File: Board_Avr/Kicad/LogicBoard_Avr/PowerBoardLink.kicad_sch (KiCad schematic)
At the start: 7 parts, among them J4 Power Board Connector

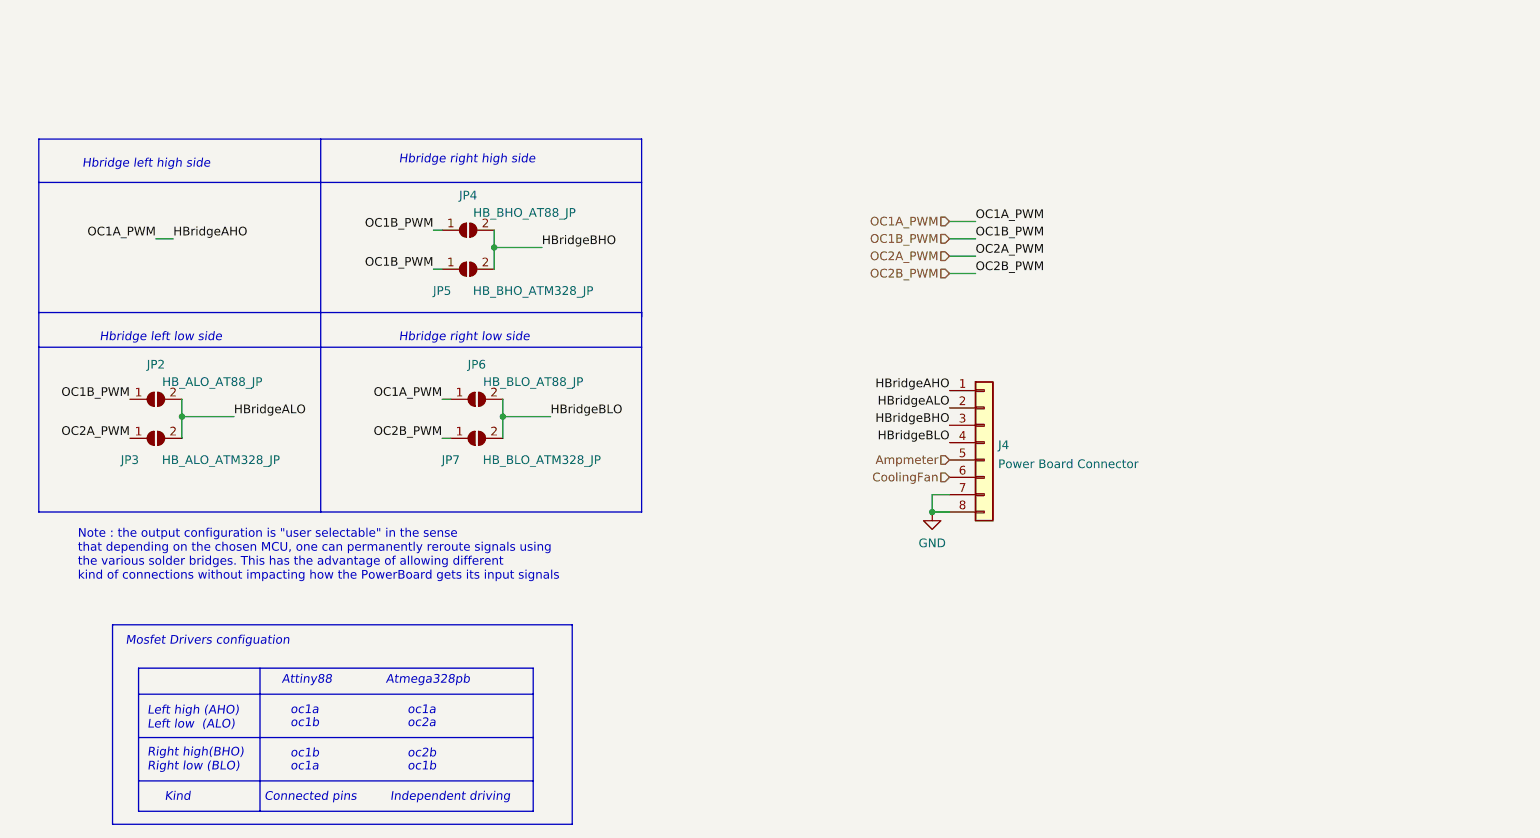
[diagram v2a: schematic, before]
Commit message: Started routing all traces
Signed-off-by: bebenlebricolo <benoittarrade@hotmail.fr>
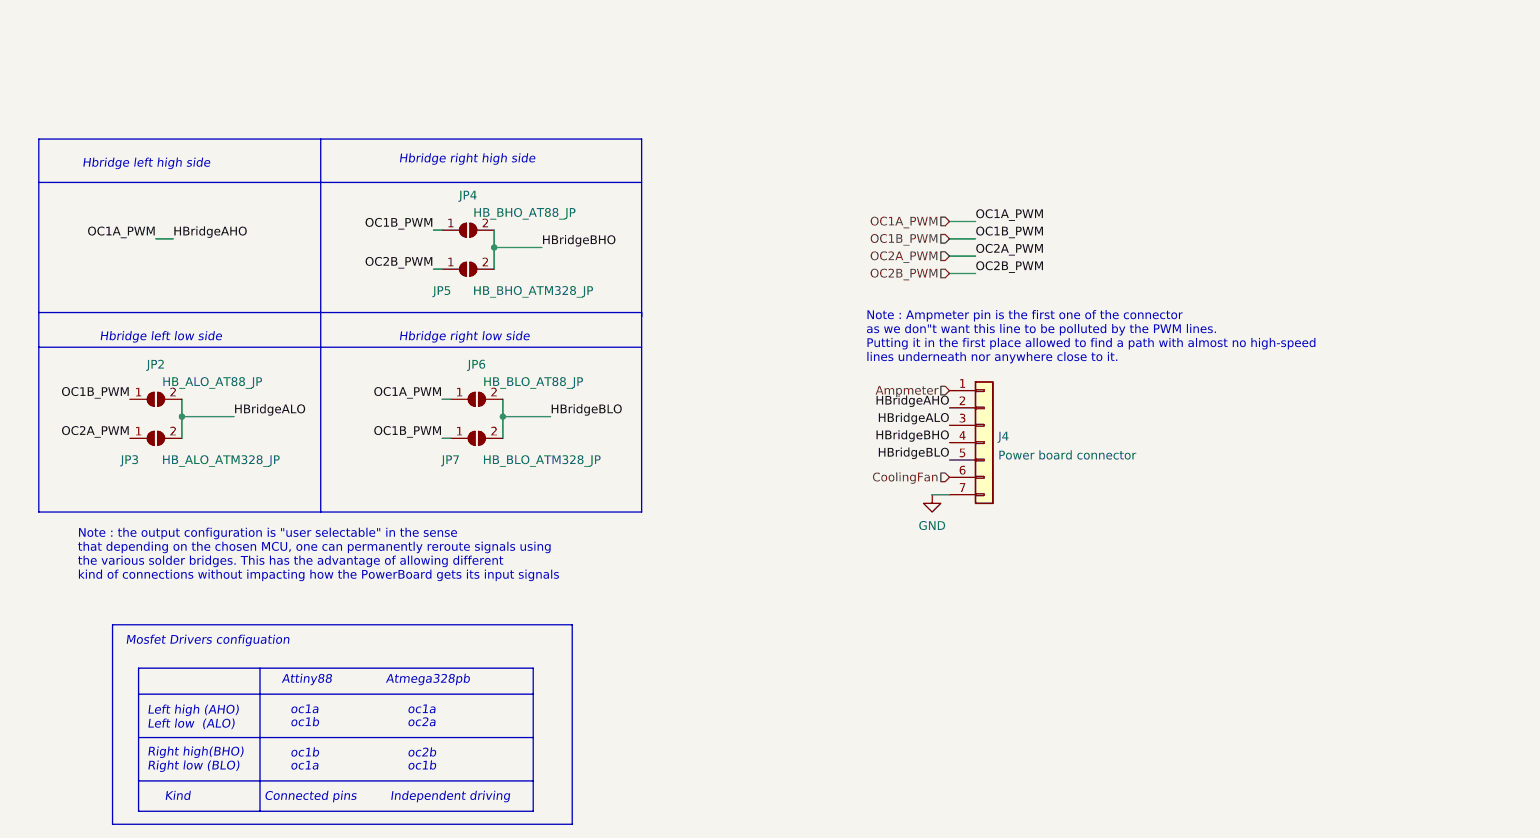
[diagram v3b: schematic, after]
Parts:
- removed J4: Power Board Connector, symbol Connector_Generic:Conn_01x08
- added J4: Power board connector, Connector_PinHeader_2.54mm:PinHeader_1x07_P2.54mm_Vertical, symbol Connector_Generic:Conn_01x07
- JP2, JP3, JP4, JP5, JP6, JP7: footprint (none) -> Jumper:SolderJumper-2_P1.3mm_Open_RoundedPad1.0x1.5mm
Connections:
- net Ampmeter: now also J4.1 (Pin_1)
- net CoolingFan: now also J4.6 (Pin_6)
- net GND: now also J4.7 (Pin_7)
- net HBridgeALO: now also J4.3 (Pin_3)
- net HBridgeBHO: now also J4.4 (Pin_4)
- net HBridgeBLO: now also J4.5 (Pin_5)
- net OC1A_PWM: now also J4.2 (Pin_2)
- net OC1B_PWM: now also JP7.1 (A); no longer JP5.1 (A)
- net OC2B_PWM: now also JP5.1 (A); no longer JP7.1 (A)
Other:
- note added: "Note : Ampmeter pin is the first one of the connector as we don"t want this line to be polluted by the PWM lines. Putting it in the first place allowed to find a path with almost no high-speed lines underneath nor anywhere close to it."
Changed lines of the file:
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@@
   (junction (at 98.425 48.895) (diameter 0) (color 0 0 0 0)
   )
-  (junction (at 162.56 87.63) (diameter 0) (color 0 0 0 0)
-  )
   (junction (at 52.705 73.66) (diameter 0) (color 0 0 0 0)
   )
@@
     (stroke (width 0) (type default) (color 0 0 0 0))
   )
-  (wire (pts (xy 162.56 87.63) (xy 165.1 87.63))
+  (wire (pts (xy 162.56 85.09) (xy 165.1 85.09))
     (stroke (width 0) (type default) (color 0 0 0 0))
   )
@@
     (stroke (width 0) (type default) (color 0 0 0 0))
   )
-  (wire (pts (xy 162.56 85.09) (xy 162.56 87.63))
-    (stroke (width 0) (type default) (color 0 0 0 0))
-  )
   (wire (pts (xy 90.805 71.12) (xy 92.075 71.12))
     (stroke (width 0) (type default) (color 0 0 0 0))
@@
   )
   (wire (pts (xy 165.1 52.705) (xy 168.91 52.705))
-    (stroke (width 0) (type default) (color 0 0 0 0))
-  )
-  (wire (pts (xy 165.1 85.09) (xy 162.56 85.09))
     (stroke (width 0) (type default) (color 0 0 0 0))
   )
@@
     (effects (font (size 1.27 1.27) italic) (justify left bottom))
   )
+  (text "Note : Ampmeter pin is the first one of the connector\nas we don\"t want this line to be polluted by the PWM lines.\nPutting it in the first place allowed to find a path with almost no high-speed \nlines underneath nor anywhere close to it."
+    (at 152.908 65.913 0)
+    (effects (font (size 1.27 1.27)) (justify left bottom))
+  )
   (text "oc1b" (at 68.58 119.38 0)
     (effects (font (size 1.27 1.27) italic) (justify left bottom))
@@
     (effects (font (size 1.27 1.27)) (justify left bottom))
   )
-  (label "HBridgeALO" (at 165.1 72.39 180)
+  (label "HBridgeALO" (at 165.1 74.93 180)
     (effects (font (size 1.27 1.27)) (justify right bottom))
   )
@@
     (effects (font (size 1.27 1.27)) (justify left bottom))
   )
-  (label "HBridgeAHO" (at 165.1 69.85 180)
+  (label "HBridgeAHO" (at 165.1 72.39 180)
     (effects (font (size 1.27 1.27)) (justify right bottom))
   )
@@
     (effects (font (size 1.27 1.27)) (justify left bottom))
   )
-  (label "OC2B_PWM" (at 90.805 76.835 180)
+  (label "OC2B_PWM" (at 89.535 52.07 180)
     (effects (font (size 1.27 1.27)) (justify right bottom))
   )
@@
     (effects (font (size 1.27 1.27)) (justify right bottom))
   )
+  (label "OC1B_PWM" (at 90.805 76.835 180)
+    (effects (font (size 1.27 1.27)) (justify right bottom))
+  )
   (label "OC1B_PWM" (at 89.535 46.355 180)
     (effects (font (size 1.27 1.27)) (justify right bottom))
@@
     (effects (font (size 1.27 1.27)) (justify right bottom))
   )
-  (label "HBridgeBLO" (at 165.1 77.47 180)
-    (effects (font (size 1.27 1.27)) (justify right bottom))
-  )
-  (label "HBridgeBHO" (at 165.1 74.93 180)
-    (effects (font (size 1.27 1.27)) (justify right bottom))
-  )
-  (label "OC1B_PWM" (at 89.535 52.07 180)
+  (label "HBridgeBLO" (at 165.1 80.01 180)
+    (effects (font (size 1.27 1.27)) (justify right bottom))
+  )
+  (label "HBridgeBHO" (at 165.1 77.47 180)
     (effects (font (size 1.27 1.27)) (justify right bottom))
   )
@@
     (effects (font (size 1.27 1.27)) (justify right))
   )
-  (hierarchical_label "Ampmeter" (shape input) (at 165.1 80.01 180)
+  (hierarchical_label "Ampmeter" (shape input) (at 165.1 69.85 180)
     (effects (font (size 1.27 1.27)) (justify right))
   )
@@
     (property "Reference" "JP6" (id 0) (at 95.885 66.04 0))
     (property "Value" "HB_BLO_AT88_JP" (id 1) (at 104.14 68.58 0))
-    (property "Footprint" "" (id 2) (at 95.885 71.12 0)
+    (property "Footprint" "Jumper:SolderJumper-2_P1.3mm_Open_RoundedPad1.0x1.5mm" (id 2) (at 95.885 71.12 0)
       (effects (font (size 1.27 1.27)) hide)
     )
@@
     (property "Reference" "JP7" (id 0) (at 92.075 80.01 0))
     (property "Value" "HB_BLO_ATM328_JP" (id 1) (at 105.41 80.01 0))
-    (property "Footprint" "" (id 2) (at 95.885 76.835 0)
+    (property "Footprint" "Jumper:SolderJumper-2_P1.3mm_Open_RoundedPad1.0x1.5mm" (id 2) (at 95.885 76.835 0)
       (effects (font (size 1.27 1.27)) hide)
     )
@@
     (pin "2")
   )
-  (symbol (lib_id "Jumper:SolderJumper_2_Open") (at 94.615 46.355 0) (unit 1)
-    (in_bom yes) (on_board yes)
-    (property "Reference" "JP4" (id 0) (at 94.615 41.275 0))
-    (property "Value" "HB_BHO_AT88_JP" (id 1) (at 102.87 43.815 0))
-    (property "Footprint" "" (id 2) (at 94.615 46.355 0)
-      (effects (font (size 1.27 1.27)) hide)
-    )
-    (property "Datasheet" "~" (id 3) (at 94.615 46.355 0)
-      (effects (font (size 1.27 1.27)) hide)
-    )
-    (pin "1")
-    (pin "2")
-  )
-  (symbol (lib_id "Connector_Generic:Conn_01x08") (at 170.18 77.47 0) (unit 1)
+  (symbol (lib_id "Connector_Generic:Conn_01x07") (at 170.18 77.47 0) (unit 1)
     (in_bom yes) (on_board yes) (fields_autoplaced)
-    (property "Reference" "J4" (id 0) (at 172.212 77.8315 0)
+    (property "Reference" "J4" (id 0) (at 172.212 76.5615 0)
       (effects (font (size 1.27 1.27)) (justify left))
     )
-    (property "Value" "Power Board Connector" (id 1) (at 172.212 80.6066 0)
+    (property "Value" "Power board connector" (id 1) (at 172.212 79.3366 0)
       (effects (font (size 1.27 1.27)) (justify left))
     )
-    (property "Footprint" "" (id 2) (at 170.18 77.47 0)
+    (property "Footprint" "Connector_PinHeader_2.54mm:PinHeader_1x07_P2.54mm_Vertical" (id 2) (at 170.18 77.47 0)
       (effects (font (size 1.27 1.27)) hide)
     )
@@
     (pin "6")
     (pin "7")
-    (pin "8")
+  )
+  (symbol (lib_id "Jumper:SolderJumper_2_Open") (at 94.615 46.355 0) (unit 1)
+    (in_bom yes) (on_board yes)
+    (property "Reference" "JP4" (id 0) (at 94.615 41.275 0))
+    (property "Value" "HB_BHO_AT88_JP" (id 1) (at 102.87 43.815 0))
+    (property "Footprint" "Jumper:SolderJumper-2_P1.3mm_Open_RoundedPad1.0x1.5mm" (id 2) (at 94.615 46.355 0)
+      (effects (font (size 1.27 1.27)) hide)
+    )
+    (property "Datasheet" "~" (id 3) (at 94.615 46.355 0)
+      (effects (font (size 1.27 1.27)) hide)
+    )
+    (pin "1")
+    (pin "2")
   )
   (symbol (lib_id "Jumper:SolderJumper_2_Open") (at 94.615 52.07 0) (unit 1)
@@
     (property "Reference" "JP5" (id 0) (at 90.805 55.245 0))
     (property "Value" "HB_BHO_ATM328_JP" (id 1) (at 104.14 55.245 0))
-    (property "Footprint" "" (id 2) (at 94.615 52.07 0)
+    (property "Footprint" "Jumper:SolderJumper-2_P1.3mm_Open_RoundedPad1.0x1.5mm" (id 2) (at 94.615 52.07 0)
       (effects (font (size 1.27 1.27)) hide)
     )
@@
     (property "Reference" "JP2" (id 0) (at 48.895 66.04 0))
     (property "Value" "HB_ALO_AT88_JP" (id 1) (at 57.15 68.58 0))
-    (property "Footprint" "" (id 2) (at 48.895 71.12 0)
+    (property "Footprint" "Jumper:SolderJumper-2_P1.3mm_Open_RoundedPad1.0x1.5mm" (id 2) (at 48.895 71.12 0)
       (effects (font (size 1.27 1.27)) hide)
     )
@@
     (property "Reference" "JP3" (id 0) (at 45.085 80.01 0))
     (property "Value" "HB_ALO_ATM328_JP" (id 1) (at 58.42 80.01 0))
-    (property "Footprint" "" (id 2) (at 48.895 76.835 0)
+    (property "Footprint" "Jumper:SolderJumper-2_P1.3mm_Open_RoundedPad1.0x1.5mm" (id 2) (at 48.895 76.835 0)
       (effects (font (size 1.27 1.27)) hide)
     )
@@
     (pin "2")
   )
-  (symbol (lib_id "power:GND") (at 162.56 87.63 0) (unit 1)
+  (symbol (lib_id "power:GND") (at 162.56 85.09 0) (unit 1)
     (in_bom yes) (on_board yes) (fields_autoplaced)
-    (property "Reference" "#PWR0130" (id 0) (at 162.56 93.98 0)
-      (effects (font (size 1.27 1.27)) hide)
-    )
-    (property "Value" "GND" (id 1) (at 162.56 92.1925 0))
-    (property "Footprint" "" (id 2) (at 162.56 87.63 0)
-      (effects (font (size 1.27 1.27)) hide)
-    )
-    (property "Datasheet" "" (id 3) (at 162.56 87.63 0)
-      (effects (font (size 1.27 1.27)) hide)
-    )
+    (property "Reference" "#PWR0130" (id 0) (at 162.56 91.44 0)
+      (effects (font (size 1.27 1.27)) hide)
+    )
+    (property "Value" "GND" (id 1) (at 162.56 89.6525 0))
+    (property "Footprint" "" (id 2) (at 162.56 85.09 0)
+      (effects (font (size 1.27 1.27)) hide)
+    )
+    (property "Datasheet" "" (id 3) (at 162.56 85.09 0)
+      (effects (font (size 1.27 1.27)) hide)
+    )
